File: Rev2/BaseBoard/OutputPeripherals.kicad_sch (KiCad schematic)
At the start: 4 parts, among them J2 Conn_01x03_Socket, J5 Conn_01x04_Socket

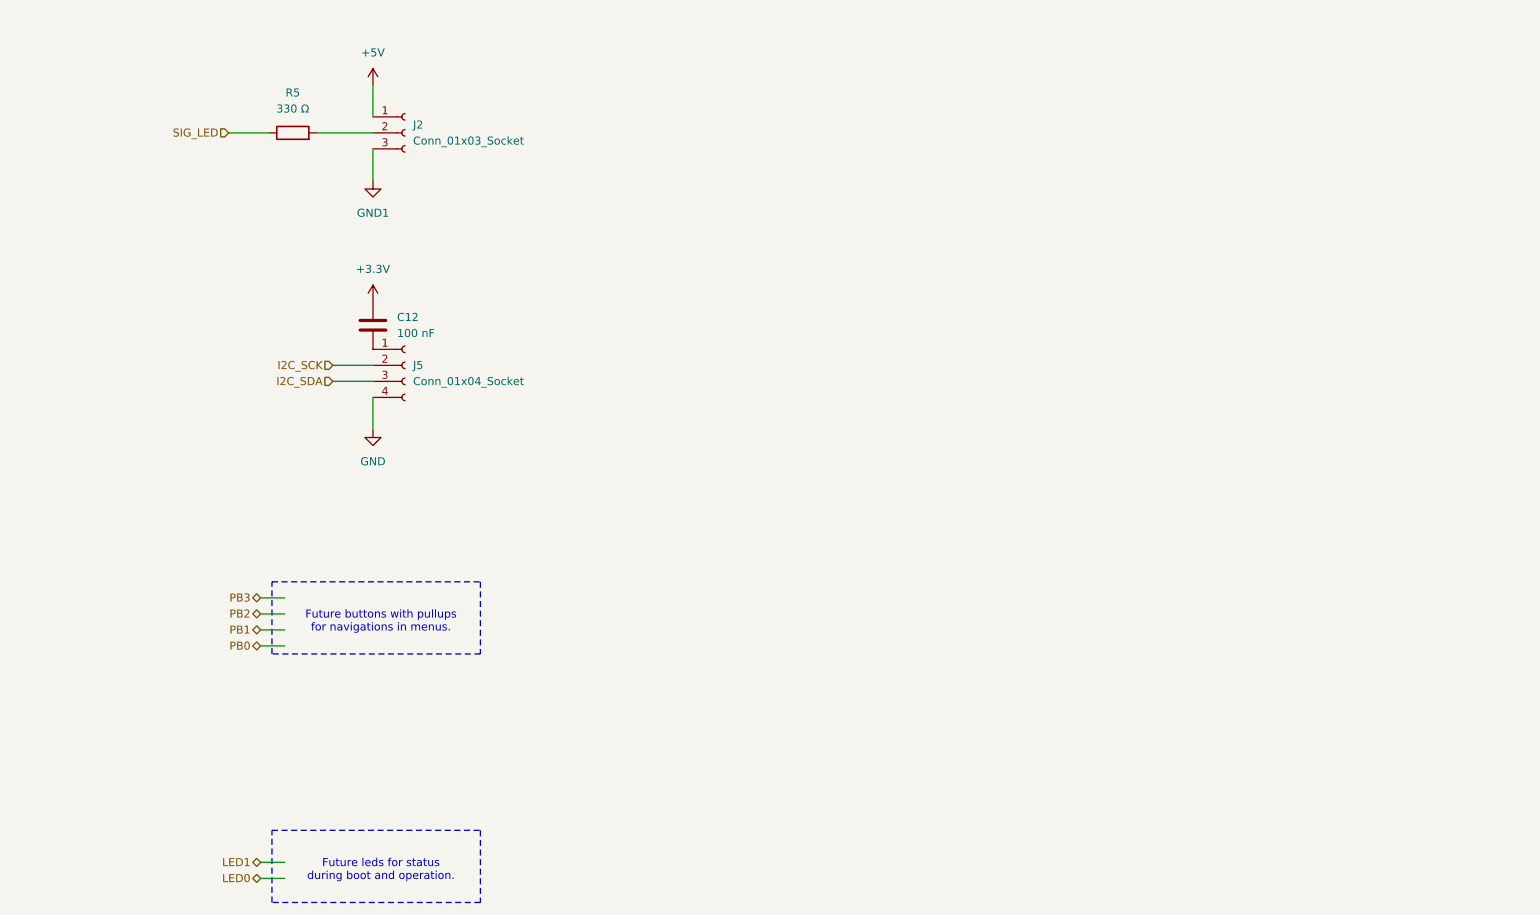
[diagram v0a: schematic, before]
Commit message: Added Testpoints, UART and JTAG
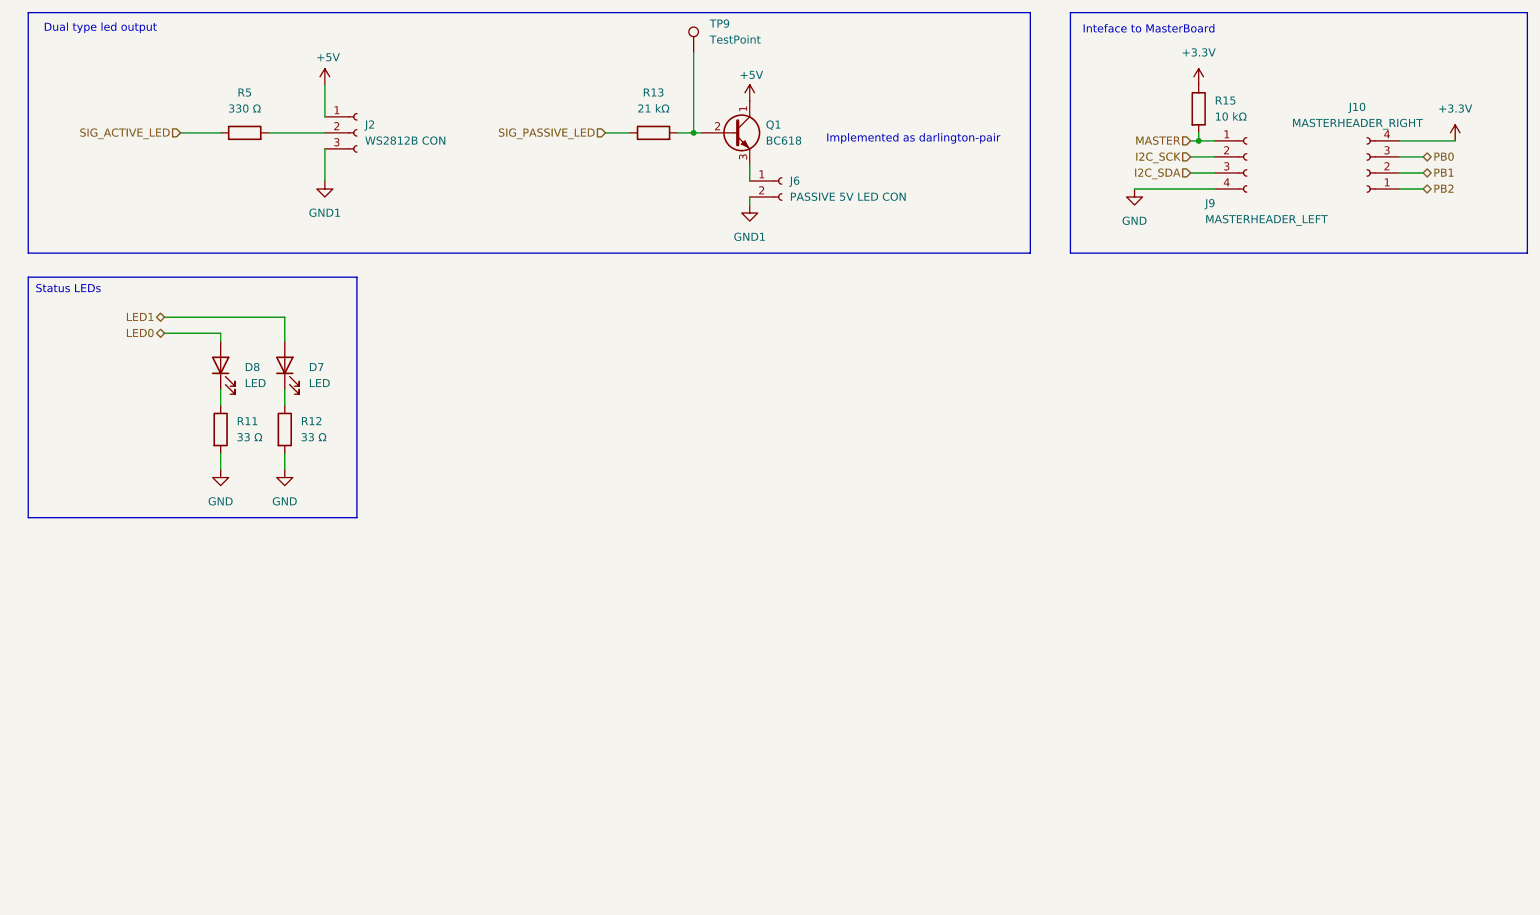
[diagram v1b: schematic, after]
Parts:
- removed C12: 100 nF, symbol Device:C
- removed J5: Conn_01x04_Socket, symbol Connector:Conn_01x04_Socket
- added D7, D8: LED, LED_SMD:LED_0805_2012Metric_Pad1.15x1.40mm_HandSolder, symbol Device:LED
- added J10: MASTERHEADER_RIGHT, Connector_PinSocket_2.54mm:PinSocket_1x04_P2.54mm_Vertical, symbol Connector:Conn_01x04_Socket
- added J6: PASSIVE 5V LED CON, Connector_PinSocket_2.54mm:PinSocket_1x02_P2.54mm_Vertical, symbol Connector:Conn_01x02_Socket
- added J9: MASTERHEADER_LEFT, Connector_PinSocket_2.54mm:PinSocket_1x04_P2.54mm_Vertical, symbol Connector:Conn_01x04_Socket
- added Q1: BC618, Package_TO_SOT_THT:TO-92_Inline, symbol Transistor_BJT:BC337
- added R11, R12: 33 Ω, symbol Device:R
- added R13: 21 kΩ, symbol Device:R
- added R15: 10 kΩ, symbol Device:R
- added TP9: TestPoint, symbol Connector:TestPoint
- J2: value Conn_01x03_Socket -> WS2812B CON
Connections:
- net +3.3V: now also J10.4 (Pin_4), R15.1
- net +5V: now also Q1.1 (C)
- net GND: now also J9.4 (Pin_4), R11.2, R12.2
- net GND1: now also J6.2 (Pin_2)
- net I2C_SCK: now also J9.2 (Pin_2)
- net I2C_SDA: now also J9.3 (Pin_3)
- net LED0: now also D8.2 (A)
- net LED1: now also D7.2 (A)
- net PB0: now also J10.3 (Pin_3)
- net PB1: now also J10.2 (Pin_2)
- net PB2: now also J10.1 (Pin_1)
- net SIG_LED renamed SIG_ACTIVE_LED
- new net: D8.1 (K), R11.1
- new net: Q1.2 (B), R13.2, TP9.1
- new net: J6.1 (Pin_1), Q1.3 (E)
- new net: D7.1 (K), R12.1
- new net MASTER: J9.1 (Pin_1), R15.2
- new net SIG_PASSIVE_LED: R13.1
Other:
- note added: "Dual type led output"
- note added: "Implemented as darlington-pair"
- note added: "Inteface to MasterBoard"
- note added: "Status LEDs"
- note removed: "Future buttons with pullups for navigations in menus."
- note removed: "Future leds for status during boot and operation."
- moved on the sheet: J2, R5

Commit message: Finished placement, routing remains
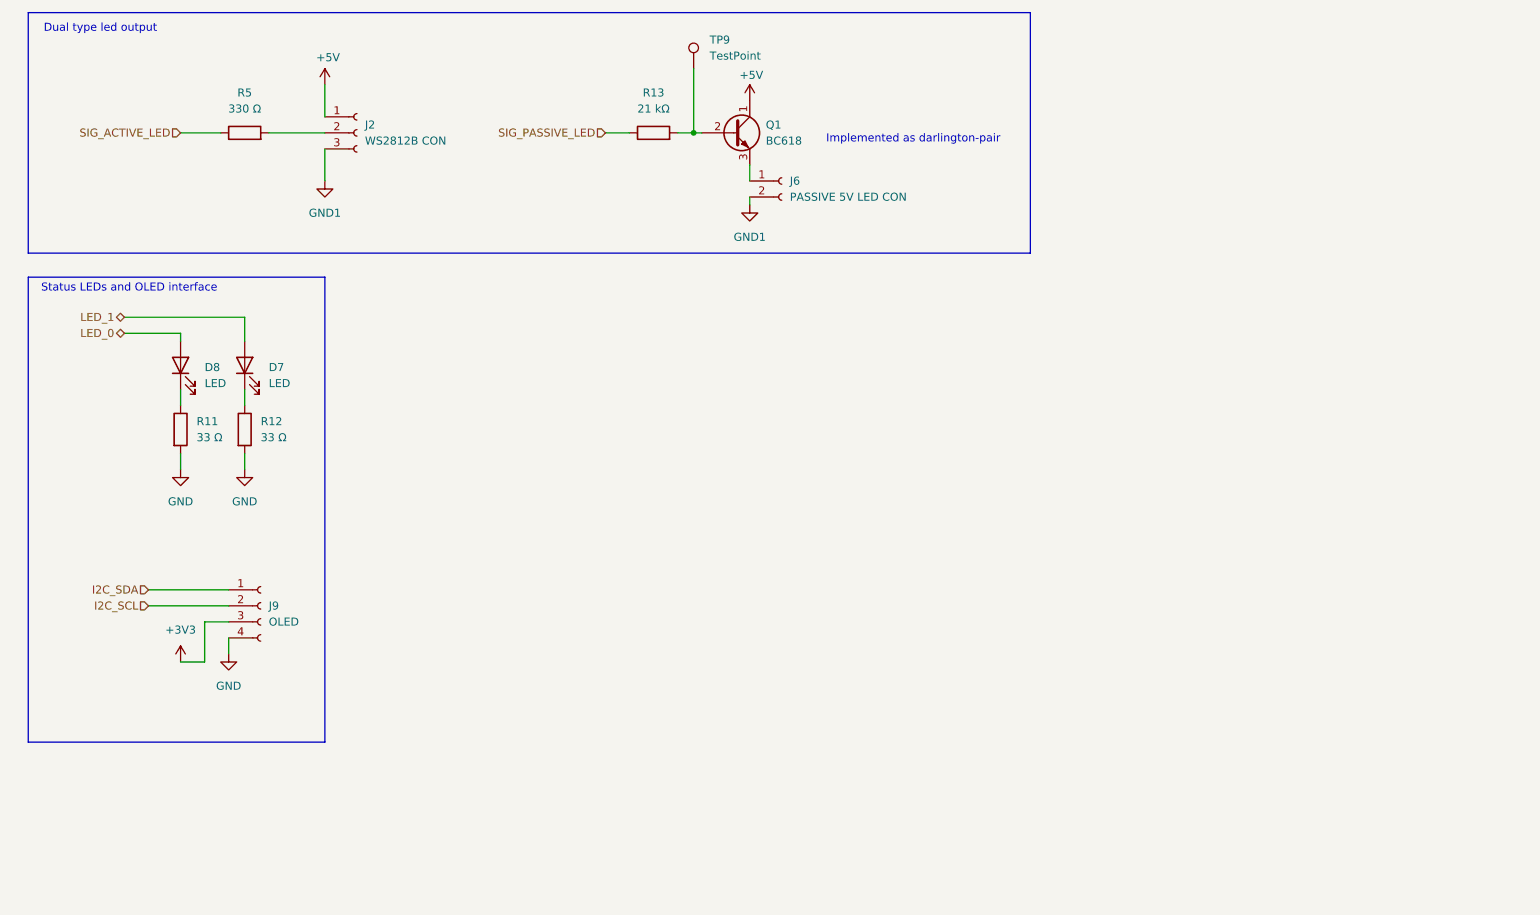
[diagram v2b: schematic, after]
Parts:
- removed J10: MASTERHEADER_RIGHT, Connector_PinSocket_2.54mm:PinSocket_1x04_P2.54mm_Vertical, symbol Connector:Conn_01x04_Socket
- removed R15: 10 kΩ, symbol Device:R
- J2: footprint (none) -> Connector_PinSocket_2.54mm:PinSocket_1x03_P2.54mm_Vertical
- J9: value MASTERHEADER_LEFT -> OLED
- R11, R12, R13, R5: footprint (none) -> Resistor_SMD:R_0805_2012Metric_Pad1.20x1.40mm_HandSolder
- TP9: footprint (none) -> TestPoint:TestPoint_Pad_1.0x1.0mm
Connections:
- net MASTER is gone; now on net I2C_SDA: J9.1 (Pin_1)
- net I2C_SDA: no longer J9.3 (Pin_3)
- net I2C_SCK renamed I2C_SCL
- net LED0 renamed LED_0
- net LED1 renamed LED_1
- new net +3V3: J9.3 (Pin_3)
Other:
- note added: "Status LEDs and OLED interface"
- note removed: "Inteface to MasterBoard"
- note removed: "Status LEDs"
- moved on the sheet: D7, D8, R11, R12, TP9
